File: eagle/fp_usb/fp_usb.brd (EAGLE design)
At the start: 77.6 x 26.6 mm, 6 parts, among them J3 USB-B-S-F-B-TH, J4 87583-3010RPALF, J5 TSM-105-01-S-SV

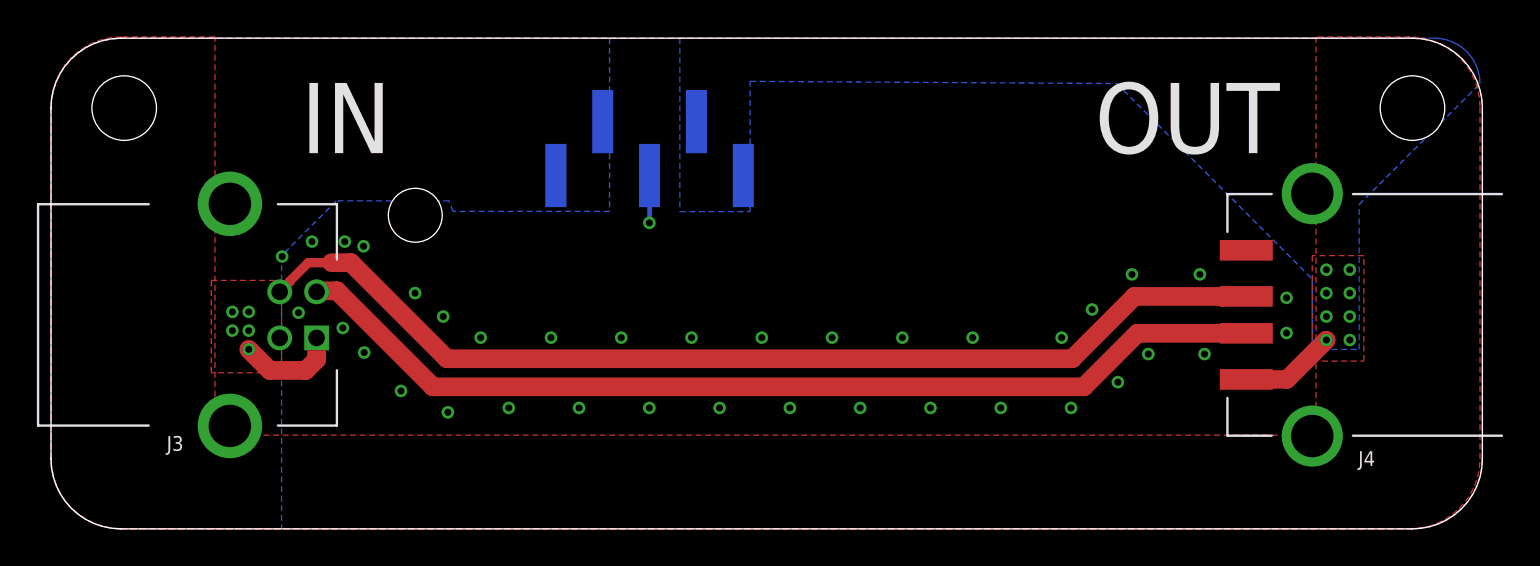
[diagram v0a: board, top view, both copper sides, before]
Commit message: Pre-production update.
* Increased clearances from chassis/enclosure ground.
* Improved text.
* Added gerbers.
* Added USB back panel.
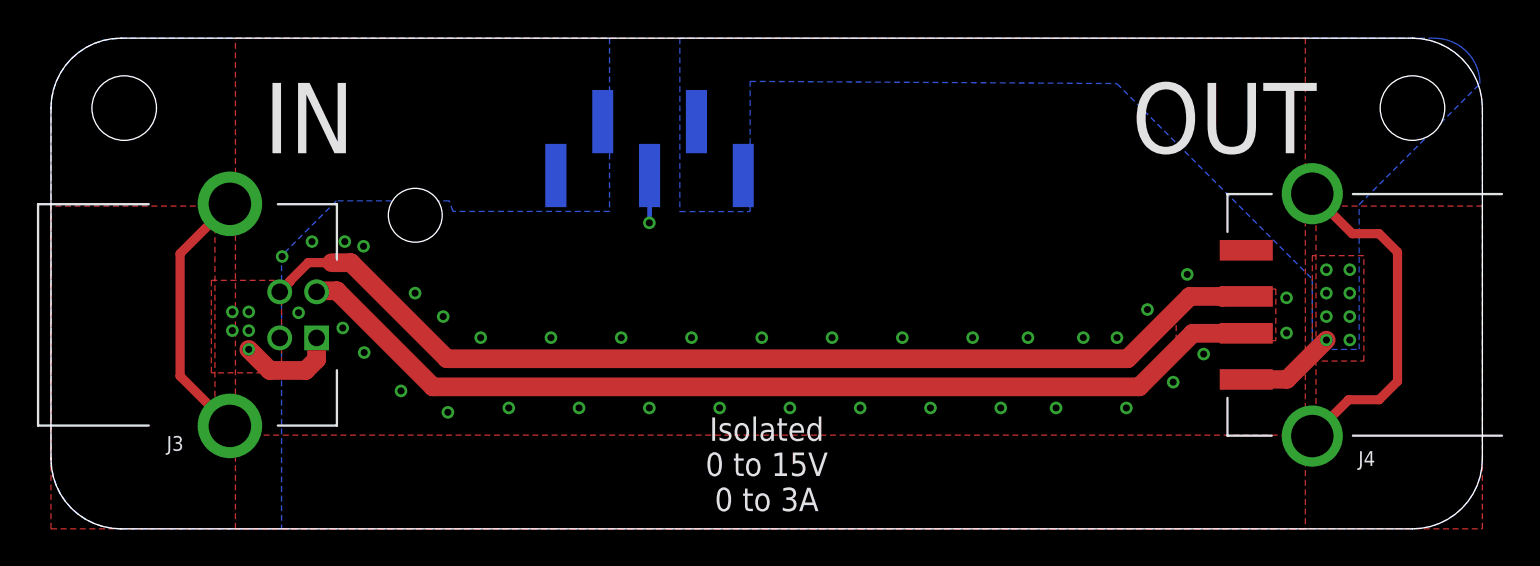
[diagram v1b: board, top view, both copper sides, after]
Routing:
- net SHIELD: track 0.00 -> 33.1 mm
- net EXT_NEG: vias 38 -> 39
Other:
- board text added: "Isolated 0 to 15V 0 to 3A"
- board text added: "Joulescope Front Panel: USB rev C 2019 Jetperch LLC"
- board text removed: "Joulescope Front Panel: USB rev B c 2018 Jetperch LLC"
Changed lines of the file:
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@@
 <?xml version="1.0" encoding="utf-8"?>
 <!DOCTYPE eagle SYSTEM "eagle.dtd">
-<eagle version="9.2.2">
+<eagle version="9.3.2">
 <drawing>
 <settings>
@@
 <setting verticaltext="up"/>
 </settings>
-<grid distance="0.01" unitdist="inch" unit="inch" style="lines" multiple="1" display="no" altdistance="0.005" altunitdist="inch" altunit="inch"/>
+<grid distance="1" unitdist="mm" unit="mm" style="lines" multiple="1" display="no" altdistance="0.1" altunitdist="mm" altunit="mm"/>
 <layers>
 <layer number="1" name="Top" color="4" fill="1" visible="yes" active="yes"/>
@@
 <wire x1="73.81" y1="26.6" x2="3.79" y2="26.6" width="0" layer="20"/>
 <wire x1="3.79" y1="26.6" x2="0" y2="22.81" width="0" layer="20" curve="90"/>
-<text x="16" y="22.27" size="3.81" layer="121" font="vector" ratio="20" align="center">IN</text>
-<text x="61.6" y="22.27" size="3.81" layer="121" font="vector" ratio="20" align="center">OUT</text>
-<text x="38.8" y="3.01" size="1.27" layer="122" font="vector" ratio="20" rot="MR0" align="center">Joulescope Front Panel: USB rev B
- c  2018 Jetperch LLC</text>
-<circle x="46.99" y="1.867" radius="1.016" width="0.254" layer="122"/>
+<text x="14" y="22.27" size="3.81" layer="121" font="vector" ratio="20" align="center">IN</text>
+<text x="63.6" y="22.27" size="3.81" layer="121" font="vector" ratio="20" align="center">OUT</text>
+<text x="38.8" y="3.01" size="1.27" layer="122" font="vector" ratio="20" rot="MR0" align="center">Joulescope Front Panel: USB rev C
+2019 Jetperch LLC</text>
 <dimension x1="0" y1="22.81" x2="77.6" y2="19.05" x3="38.8" y3="31.75" textsize="1.778" layer="47" dtype="horizontal"/>
 <dimension x1="3.79" y1="0" x2="7.62" y2="26.6" x3="-6.35" y3="13.3" textsize="1.778" layer="47" dtype="vertical"/>
@@
 <rectangle x1="0" y1="0" x2="1.5" y2="26.6" layer="40"/>
 <rectangle x1="76.1" y1="0" x2="77.6" y2="26.6" layer="40"/>
+<text x="38.8" y="3.5" size="1.27" layer="121" font="vector" ratio="20" align="center">Isolated
+0 to 15V
+0 to 3A</text>
 </plain>
 <attributes>
@@
 <signal name="EXT_NEG">
 <polygon width="0.254" layer="1" isolate="0.254" thermals="no" rank="3">
-<vertex x="3.79" y="26.6"/>
-<vertex x="73.81" y="26.6" curve="-90"/>
-<vertex x="77.6" y="22.81"/>
-<vertex x="77.6" y="3.79" curve="-90"/>
-<vertex x="73.81" y="0"/>
-<vertex x="3.79" y="0" curve="-90"/>
-<vertex x="0" y="3.79"/>
-<vertex x="0" y="22.81" curve="-90"/>
+<vertex x="68" y="0"/>
+<vertex x="10" y="0"/>
+<vertex x="10" y="26.6"/>
+<vertex x="68" y="26.6"/>
 </polygon>
 <contactref element="J3" pad="4"/>
@@
 <via x="47.679" y="6.555" extent="1-16" drill="0.381"/>
 <via x="51.489" y="6.555" extent="1-16" drill="0.381"/>
-<via x="55.299" y="6.555" extent="1-16" drill="0.381"/>
-<via x="57.839" y="7.952" extent="1-16" drill="0.381"/>
-<via x="59.49" y="9.476" extent="1-16" drill="0.381"/>
-<via x="62.538" y="9.476" extent="1-16" drill="0.381"/>
-<via x="62.284" y="13.794" extent="1-16" drill="0.381"/>
-<via x="58.601" y="13.794" extent="1-16" drill="0.381"/>
-<via x="54.791" y="10.365" extent="1-16" drill="0.381"/>
-<via x="56.442" y="11.889" extent="1-16" drill="0.381"/>
+<via x="58.299" y="6.555" extent="1-16" drill="0.381"/>
+<via x="60.839" y="7.952" extent="1-16" drill="0.381"/>
+<via x="62.49" y="9.476" extent="1-16" drill="0.381"/>
+<via x="61.601" y="13.794" extent="1-16" drill="0.381"/>
+<via x="57.791" y="10.365" extent="1-16" drill="0.381"/>
+<via x="59.442" y="11.889" extent="1-16" drill="0.381"/>
 <via x="27.105" y="10.365" extent="1-16" drill="0.381"/>
 <via x="30.915" y="10.365" extent="1-16" drill="0.381"/>
@@
 <via x="16.979" y="9.557" extent="1-16" drill="0.381"/>
 <via x="16.945" y="15.318" extent="1-16" drill="0.381"/>
+<via x="52.965" y="10.365" extent="1-16" drill="0.381"/>
+<via x="54.489" y="6.555" extent="1-16" drill="0.381"/>
+<via x="55.965" y="10.365" extent="1-16" drill="0.381"/>
+<polygon width="0.254" layer="1" pour="cutout">
+<vertex x="66.4" y="13"/>
+<vertex x="66.4" y="10.2"/>
+<vertex x="61" y="10.2"/>
+<vertex x="61" y="12"/>
+<vertex x="62" y="13"/>
+</polygon>
 </signal>
 <signal name="EXT_OUT">
@@
 <contactref element="J4" pad="SHIELD@1"/>
 <polygon width="0.254" layer="1" isolate="0.254" rank="2">
-<vertex x="8.89" y="26.67"/>
-<vertex x="3.79" y="26.67" curve="90"/>
-<vertex x="0" y="22.88"/>
-<vertex x="0" y="3.79" curve="90"/>
-<vertex x="3.79" y="0"/>
-<vertex x="73.68" y="0" curve="90"/>
-<vertex x="77.47" y="3.79"/>
-<vertex x="77.47" y="22.88" curve="90"/>
-<vertex x="73.68" y="26.67"/>
-<vertex x="68.58" y="26.67"/>
+<vertex x="8.89" y="17.5"/>
+<vertex x="0" y="17.5"/>
+<vertex x="0" y="0"/>
+<vertex x="77.6" y="0"/>
+<vertex x="77.6" y="17.5"/>
+<vertex x="68.58" y="17.5"/>
 <vertex x="68.58" y="5.08"/>
 <vertex x="8.89" y="5.08"/>
 </polygon>
+<wire x1="9.7" y1="17.62" x2="7" y2="14.92" width="0.5" layer="1"/>
+<wire x1="7" y1="8.28" x2="9.7" y2="5.58" width="0.5" layer="1"/>
+<wire x1="7" y1="14.92" x2="7" y2="8.28" width="0.5" layer="1"/>
+<wire x1="68.38" y1="18.17" x2="70.55" y2="16" width="0.5" layer="1"/>
+<wire x1="70.55" y1="16" x2="72" y2="16" width="0.5" layer="1"/>
+<wire x1="73" y1="15" x2="72" y2="16" width="0.5" layer="1"/>
+<wire x1="68.38" y1="5.03" x2="70.35" y2="7" width="0.5" layer="1"/>
+<wire x1="70.35" y1="7" x2="72" y2="7" width="0.5" layer="1"/>
+<wire x1="72" y1="7" x2="73" y2="8" width="0.5" layer="1"/>
+<wire x1="73" y1="8" x2="73" y2="15" width="0.5" layer="1"/>
 </signal>
 <signal name="D_P" class="1">
 <contactref element="J3" pad="3"/>
 <contactref element="J4" pad="3"/>
-<wire x1="58.742371875" y1="12.6" x2="55.36436875" y2="9.222" width="1.016" layer="1"/>
-<wire x1="55.36436875" y1="9.222" x2="21.46763125" y2="9.222" width="1.016" layer="1"/>
+<wire x1="61.742375" y1="12.6" x2="58.36436875" y2="9.222" width="1.016" layer="1"/>
+<wire x1="58.36436875" y1="9.222" x2="21.46763125" y2="9.222" width="1.016" layer="1"/>
 <wire x1="21.46763125" y1="9.222" x2="16.26063125" y2="14.429" width="1.016" layer="1"/>
 <wire x1="16.26063125" y1="14.429" x2="15.2124375" y2="14.429" width="1.016" layer="1"/>
-<wire x1="58.742371875" y1="12.6" x2="63.462" y2="12.6" width="1.016" layer="1"/>
+<wire x1="61.742375" y1="12.6" x2="63.462" y2="12.6" width="1.016" layer="1"/>
 <wire x1="63.462" y1="12.6" x2="63.5" y2="12.562" width="1.016" layer="1"/>
 <wire x1="64.8" y1="12.6" x2="63.538" y2="12.6" width="1.016" layer="1"/>
@@
 <contactref element="J4" pad="2"/>
 <contactref element="J3" pad="2"/>
-<wire x1="58.89763125" y1="10.6" x2="55.99563125" y2="7.698" width="1.016" layer="1"/>
-<wire x1="55.99563125" y1="7.698" x2="20.70936875" y2="7.698" width="1.016" layer="1"/>
+<wire x1="61.89763125" y1="10.6" x2="58.99563125" y2="7.698" width="1.016" layer="1"/>
+<wire x1="58.99563125" y1="7.698" x2="20.70936875" y2="7.698" width="1.016" layer="1"/>
 <wire x1="20.70936875" y1="7.698" x2="15.50236875" y2="12.905" width="1.016" layer="1"/>
 <wire x1="15.50236875" y1="12.905" x2="14.455" y2="12.905" width="1.016" layer="1"/>
 <wire x1="14.455" y1="12.905" x2="14.4" y2="12.85" width="1.016" layer="1"/>
-<wire x1="58.89763125" y1="10.6" x2="64.8" y2="10.6" width="1.016" layer="1"/>
+<wire x1="61.89763125" y1="10.6" x2="64.8" y2="10.6" width="1.016" layer="1"/>
 </signal>
 </signals>

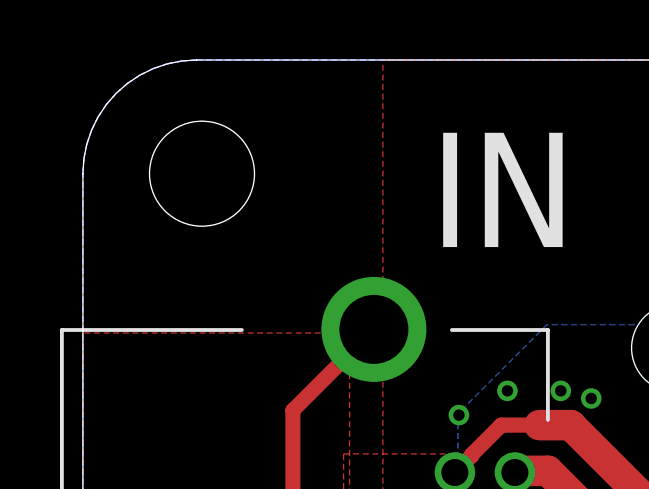
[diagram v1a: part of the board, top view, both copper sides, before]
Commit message: Fixed eagle/fp_usb mounting hole location which was off by 0.18 mm (7 mil).
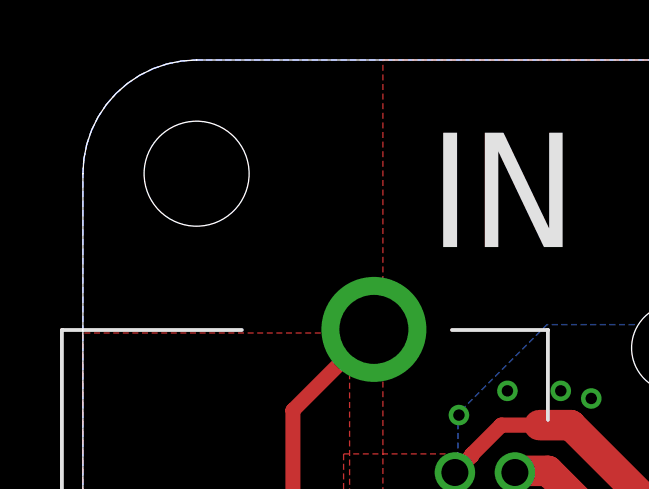
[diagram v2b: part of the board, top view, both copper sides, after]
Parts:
- moved H3 0.18 mm to (3.79, 22.8)
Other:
- board text added: "Joulescope Front Panel: USB rev D 2019 Jetperch LLC"
- board text removed: "Joulescope Front Panel: USB rev C 2019 Jetperch LLC"
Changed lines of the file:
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@@
 <?xml version="1.0" encoding="utf-8"?>
 <!DOCTYPE eagle SYSTEM "eagle.dtd">
-<eagle version="9.3.2">
+<eagle version="9.4.2">
 <drawing>
 <settings>
@@
 <text x="14" y="22.27" size="3.81" layer="121" font="vector" ratio="20" align="center">IN</text>
 <text x="63.6" y="22.27" size="3.81" layer="121" font="vector" ratio="20" align="center">OUT</text>
-<text x="38.8" y="3.01" size="1.27" layer="122" font="vector" ratio="20" rot="MR0" align="center">Joulescope Front Panel: USB rev C
+<text x="38.8" y="3.01" size="1.27" layer="122" font="vector" ratio="20" rot="MR0" align="center">Joulescope Front Panel: USB rev D
 2019 Jetperch LLC</text>
 <dimension x1="0" y1="22.81" x2="77.6" y2="19.05" x3="38.8" y3="31.75" textsize="1.778" layer="47" dtype="horizontal"/>
@@
 <attribute name="POPULATE" value="1" x="19.75" y="17" size="1.778" layer="27" display="off"/>
 </element>
-<element name="H3" library="jetperch" package="HOLE_3.5MM" value="HOLE_#6" x="3.97" y="22.81" smashed="yes">
-<attribute name="POPULATE" value="0" x="3.97" y="22.81" size="1.778" layer="27" display="off"/>
+<element name="H3" library="jetperch" package="HOLE_3.5MM" value="HOLE_#6" x="3.79" y="22.81" smashed="yes">
+<attribute name="POPULATE" value="0" x="3.79" y="22.81" size="1.778" layer="27" display="off"/>
 </element>
 <element name="H4" library="jetperch" package="HOLE_3.5MM" value="HOLE_#6" x="73.81" y="22.81" smashed="yes">
